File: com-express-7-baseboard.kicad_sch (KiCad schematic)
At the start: 0 parts

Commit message: [#57498] Add KR/SFP+
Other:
- sheet 2xSFP+ ports: added 10GKR_SFP0{10GBaseKR}, 10GKR_SFP1{10GBaseKR}, I2C_{SFP0}{I2C}, I2C_{SFP1}{I2C}, MDIO0{MDIO}, MDIO1{MDIO}, MOD0_ABS, MOD1_ABS, PHY0_{RESET}, PHY1_{RESET}; removed 10GKR_A{10GBaseKR}, 10GKR_B{10GBaseKR}
- sheet Com Express 7 Interfaces ports: added 10G_INT0, 10G_INT1, 10G_PHY_RST01, I2C_{10GLED}{I2C}, I2C_{SFP0}{I2C}, I2C_{SFP1}{I2C}, MDIO0{MDIO}, MDIO1{MDIO}; removed none
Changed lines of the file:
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@@
   (bus_alias "10GBaseKR" (members "TX+" "TX-" "RX+" "RX-"))
   (bus_alias "GbE" (members "MDI3+" "MDI3-" "MDI2+" "MDI2-" "MDI1+" "MDI1-" "MDI0+" "MDI0-" "CTREF"))
+  (bus_alias "MDIO" (members "MDIO" "MDC"))
   (bus_alias "PCIe" (members "TX7+" "TX7-" "TX6+" "TX6-" "TX5+" "TX5-" "TX4+" "TX4-" "TX3+" "TX3-" "TX2+" "TX2-" "TX1+" "TX1-" "TX0+" "TX0-" "RX7+" "RX7-" "RX6+" "RX6-" "RX5+" "RX5-" "RX4+" "RX4-" "RX3+" "RX3-" "RX2+" "RX2-" "RX1+" "RX1-" "RX0+" "RX0-"))
   (bus_alias "USB" (members "D+" "D-"))
@@
   (junction (at 325.12 111.76) (diameter 0) (color 0 0 0 0)
   )
+  (junction (at 121.92 127) (diameter 0) (color 0 0 0 0)
+  )
   (junction (at 327.66 68.58) (diameter 0) (color 0 0 0 0)
   )
   (no_connect (at 251.46 162.56))
-  (no_connect (at 158.75 119.38))
+  (no_connect (at 158.75 97.79))
   (no_connect (at 252.73 175.26))
   (bus (pts (xy 261.62 195.58) (xy 281.94 195.58))
@@
     (stroke (width 0) (type default))
   )
-  (bus (pts (xy 119.38 114.3) (xy 162.56 114.3))
+  (bus (pts (xy 119.38 109.22) (xy 162.56 109.22))
     (stroke (width 0) (type default) (color 255 0 0 1))
   )
@@
     (stroke (width 0) (type default))
   )
+  (bus (pts (xy 119.38 116.84) (xy 162.56 116.84))
+    (stroke (width 0) (type default))
+  )
   (wire (pts (xy 121.92 86.36) (xy 162.56 86.36))
     (stroke (width 0) (type default))
@@
     (stroke (width 0) (type default))
   )
+  (wire (pts (xy 119.38 114.3) (xy 162.56 114.3))
+    (stroke (width 0) (type default))
+  )
   (wire (pts (xy 322.58 68.58) (xy 327.66 68.58))
     (stroke (width 0) (type default))
   )
   (bus (pts (xy 248.92 58.42) (xy 254 58.42))
+    (stroke (width 0) (type default))
+  )
+  (wire (pts (xy 119.38 111.76) (xy 162.56 111.76))
     (stroke (width 0) (type default))
   )
@@
     (stroke (width 0) (type default))
   )
-  (bus (pts (xy 158.75 119.38) (xy 162.56 119.38))
+  (bus (pts (xy 158.75 97.79) (xy 162.56 97.79))
     (stroke (width 0) (type default) (color 255 0 0 1))
   )
@@
     (stroke (width 0) (type default))
   )
+  (bus (pts (xy 119.38 119.38) (xy 162.56 119.38))
+    (stroke (width 0) (type default))
+  )
   (bus (pts (xy 119.38 215.9) (xy 121.92 215.9))
     (stroke (width 0) (type default))
@@
   )
   (bus (pts (xy 67.31 152.4) (xy 67.31 208.28))
+    (stroke (width 0) (type default))
+  )
+  (wire (pts (xy 119.38 127) (xy 121.92 127))
+    (stroke (width 0) (type default))
+  )
+  (wire (pts (xy 121.92 129.54) (xy 121.92 127))
     (stroke (width 0) (type default))
   )
@@
     (stroke (width 0) (type default) (color 194 0 194 1))
   )
+  (wire (pts (xy 119.38 129.54) (xy 121.92 129.54))
+    (stroke (width 0) (type default))
+  )
   (bus (pts (xy 340.36 22.86) (xy 340.36 198.12))
     (stroke (width 0) (type default))
@@
     (stroke (width 0) (type default))
   )
+  (bus (pts (xy 119.38 124.46) (xy 162.56 124.46))
+    (stroke (width 0) (type default))
+  )
   (bus (pts (xy 67.31 208.28) (xy 121.92 208.28))
+    (stroke (width 0) (type default))
+  )
+  (wire (pts (xy 121.92 127) (xy 162.56 127))
     (stroke (width 0) (type default))
   )
@@
     (stroke (width 0) (type default))
   )
+  (bus (pts (xy 119.38 121.92) (xy 162.56 121.92))
+    (stroke (width 0) (type default))
+  )
   (wire (pts (xy 327.66 33.02) (xy 327.66 45.72))
     (stroke (width 0) (type default))
@@
     (stroke (width 0) (type default))
   )
-  (bus (pts (xy 119.38 109.22) (xy 162.56 109.22))
+  (bus (pts (xy 119.38 106.68) (xy 162.56 106.68))
     (stroke (width 0) (type default) (color 255 0 0 1))
   )
@@
       (effects (font (size 1.27 1.27)) (justify left top))
     )
-    (pin "10GKR_A{10GBaseKR}" input (at 119.38 109.22 0)
-      (effects (font (size 1.27 1.27)) (justify right))
-    )
-    (pin "10GKR_B{10GBaseKR}" input (at 119.38 114.3 0)
+    (pin "I2C_{SFP0}{I2C}" input (at 119.38 116.84 0)
+      (effects (font (size 1.27 1.27)) (justify right))
+    )
+    (pin "10GKR_SFP0{10GBaseKR}" input (at 119.38 106.68 0)
+      (effects (font (size 1.27 1.27)) (justify right))
+    )
+    (pin "MOD0_ABS" output (at 119.38 111.76 0)
+      (effects (font (size 1.27 1.27)) (justify right))
+    )
+    (pin "MDIO0{MDIO}" input (at 119.38 121.92 0)
+      (effects (font (size 1.27 1.27)) (justify right))
+    )
+    (pin "PHY0_{RESET}" input (at 119.38 127 0)
+      (effects (font (size 1.27 1.27)) (justify right))
+    )
+    (pin "I2C_{SFP1}{I2C}" input (at 119.38 119.38 0)
+      (effects (font (size 1.27 1.27)) (justify right))
+    )
+    (pin "10GKR_SFP1{10GBaseKR}" input (at 119.38 109.22 0)
+      (effects (font (size 1.27 1.27)) (justify right))
+    )
+    (pin "MOD1_ABS" output (at 119.38 114.3 0)
+      (effects (font (size 1.27 1.27)) (justify right))
+    )
+    (pin "PHY1_{RESET}" input (at 119.38 129.54 0)
+      (effects (font (size 1.27 1.27)) (justify right))
+    )
+    (pin "MDIO1{MDIO}" input (at 119.38 124.46 0)
       (effects (font (size 1.27 1.27)) (justify right))
     )
@@
       (effects (font (size 1.27 1.27)) (justify right))
     )
-    (pin "KR0{10GBaseKR}" output (at 162.56 109.22 180)
-      (effects (font (size 1.27 1.27)) (justify left))
-    )
-    (pin "KR1{10GBaseKR}" output (at 162.56 114.3 180)
+    (pin "KR0{10GBaseKR}" output (at 162.56 106.68 180)
+      (effects (font (size 1.27 1.27)) (justify left))
+    )
+    (pin "KR1{10GBaseKR}" output (at 162.56 109.22 180)
       (effects (font (size 1.27 1.27)) (justify left))
     )
@@
       (effects (font (size 1.27 1.27)) (justify right))
     )
-    (pin "KR2{10GBaseKR}" output (at 162.56 119.38 180)
+    (pin "KR2{10GBaseKR}" output (at 162.56 97.79 180)
       (effects (font (size 1.27 1.27)) (justify left))
     )
@@
       (effects (font (size 1.27 1.27)) (justify left))
     )
+    (pin "10G_INT0" input (at 162.56 111.76 180)
+      (effects (font (size 1.27 1.27)) (justify left))
+    )
+    (pin "10G_INT1" input (at 162.56 114.3 180)
+      (effects (font (size 1.27 1.27)) (justify left))
+    )
+    (pin "I2C_{10GLED}{I2C}" input (at 162.56 140.97 180)
+      (effects (font (size 1.27 1.27)) (justify left))
+    )
+    (pin "I2C_{SFP1}{I2C}" output (at 162.56 119.38 180)
+      (effects (font (size 1.27 1.27)) (justify left))
+    )
+    (pin "I2C_{SFP0}{I2C}" output (at 162.56 116.84 180)
+      (effects (font (size 1.27 1.27)) (justify left))
+    )
+    (pin "MDIO1{MDIO}" output (at 162.56 124.46 180)
+      (effects (font (size 1.27 1.27)) (justify left))
+    )
+    (pin "MDIO0{MDIO}" output (at 162.56 121.92 180)
+      (effects (font (size 1.27 1.27)) (justify left))
+    )
+    (pin "10G_PHY_RST01" output (at 162.56 127 180)
+      (effects (font (size 1.27 1.27)) (justify left))
+    )

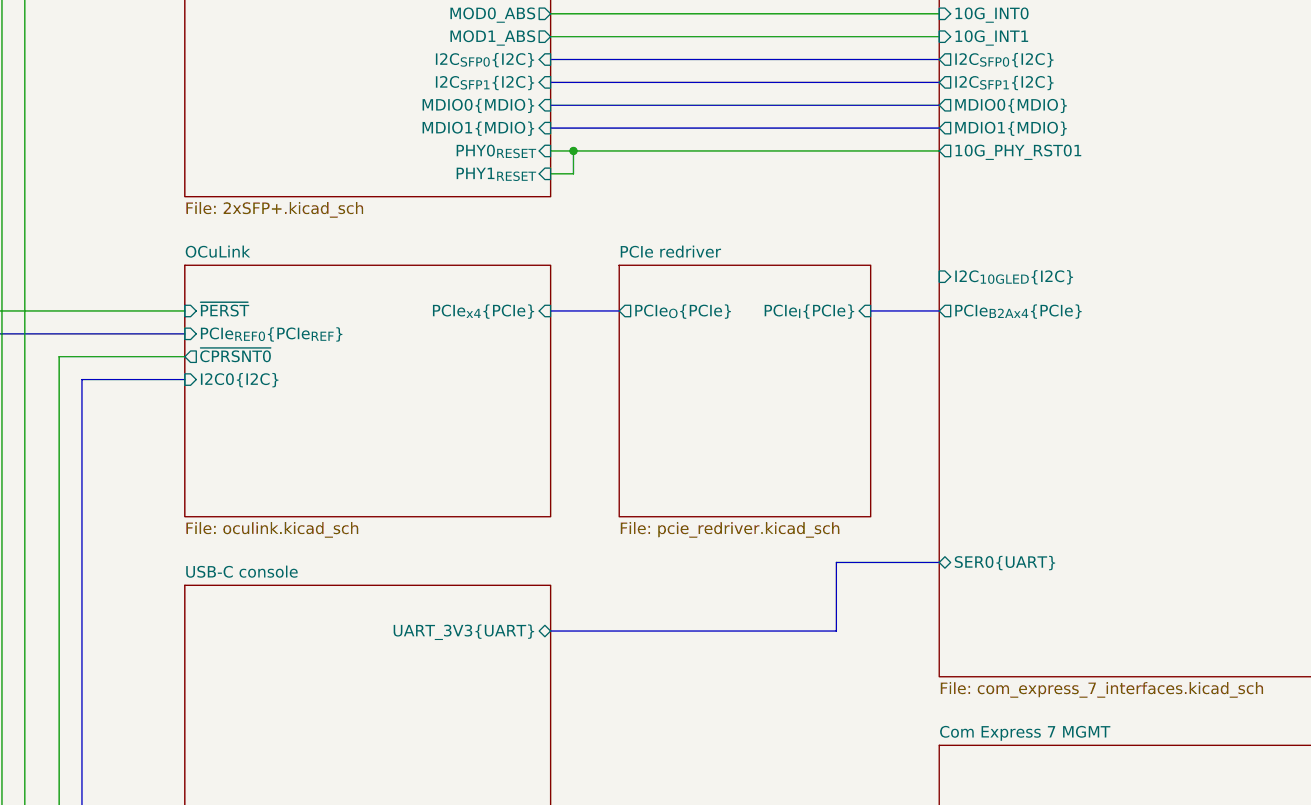
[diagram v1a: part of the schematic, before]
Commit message: [#57498] Add SFP+ indicator LEDs
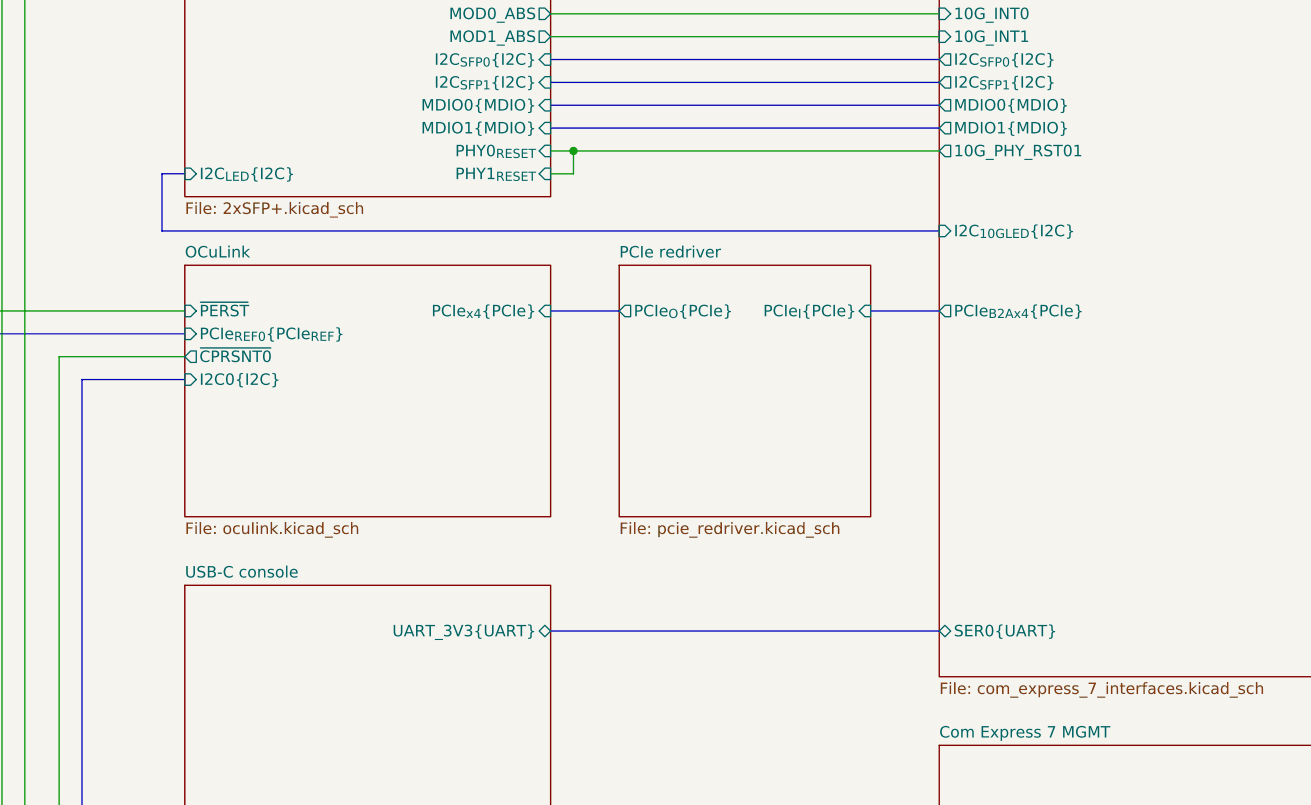
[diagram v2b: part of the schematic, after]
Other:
- sheet 2xSFP+ ports: added I2C_{LED}{I2C}; removed none
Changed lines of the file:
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@@
     (stroke (width 0) (type default))
-  )
-  (bus (pts (xy 162.56 172.72) (xy 151.13 172.72))
-    (stroke (width 0) (type default) (color 255 153 0 1))
   )
   (bus (pts (xy 261.62 177.8) (xy 261.62 195.58))
@@
     (stroke (width 0) (type default) (color 194 0 194 1))
   )
-  (bus (pts (xy 151.13 172.72) (xy 151.13 180.34))
-    (stroke (width 0) (type default) (color 255 153 0 1))
-  )
   (bus (pts (xy 52.07 22.86) (xy 52.07 147.32))
     (stroke (width 0) (type default))
@@
     (stroke (width 0) (type default))
   )
+  (bus (pts (xy 76.2 135.89) (xy 162.56 135.89))
+    (stroke (width 0) (type default))
+  )
+  (bus (pts (xy 76.2 129.54) (xy 76.2 135.89))
+    (stroke (width 0) (type default))
+  )
   (wire (pts (xy 327.66 68.58) (xy 327.66 45.72))
     (stroke (width 0) (type default))
@@
     (stroke (width 0) (type default))
   )
-  (bus (pts (xy 151.13 180.34) (xy 119.38 180.34))
+  (bus (pts (xy 119.38 180.34) (xy 162.56 180.34))
     (stroke (width 0) (type default) (color 255 153 0 1))
   )
@@
     (stroke (width 0) (type default))
   )
+  (bus (pts (xy 78.74 129.54) (xy 76.2 129.54))
+    (stroke (width 0) (type default))
+  )
   (wire (pts (xy 119.38 88.9) (xy 121.92 88.9))
     (stroke (width 0) (type default))
@@
       (effects (font (size 1.27 1.27)) (justify right))
     )
+    (pin "I2C_{LED}{I2C}" input (at 78.74 129.54 180)
+      (effects (font (size 1.27 1.27)) (justify left))
+    )
     (instances
       (project "com-express-7-baseboard"
@@
       (effects (font (size 1.27 1.27)) (justify right))
     )
-    (pin "SER0{UART}" bidirectional (at 162.56 172.72 180)
+    (pin "SER0{UART}" bidirectional (at 162.56 180.34 180)
       (effects (font (size 1.27 1.27)) (justify left))
     )
@@
       (effects (font (size 1.27 1.27)) (justify left))
     )
-    (pin "I2C_{10GLED}{I2C}" input (at 162.56 140.97 180)
-      (effects (font (size 1.27 1.27)) (justify left))
-    )
+    (pin "I2C_{10GLED}{I2C}" input (at 162.56 135.89 180)
+      (effects (font (size 1.27 1.27)) (justify left))
+    )

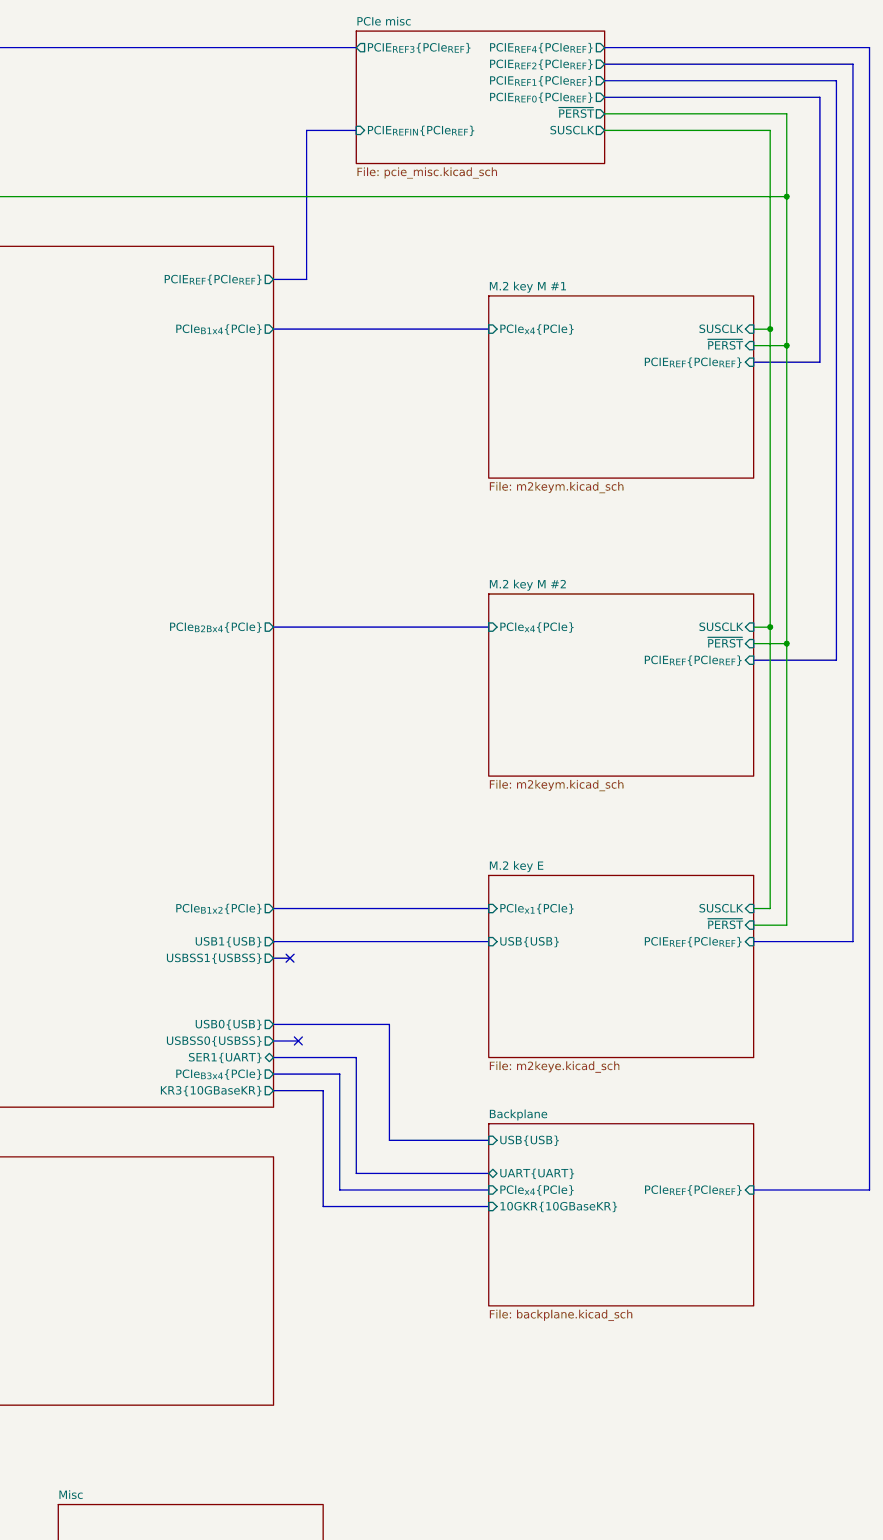
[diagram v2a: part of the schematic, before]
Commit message: [#57498] Add SD card
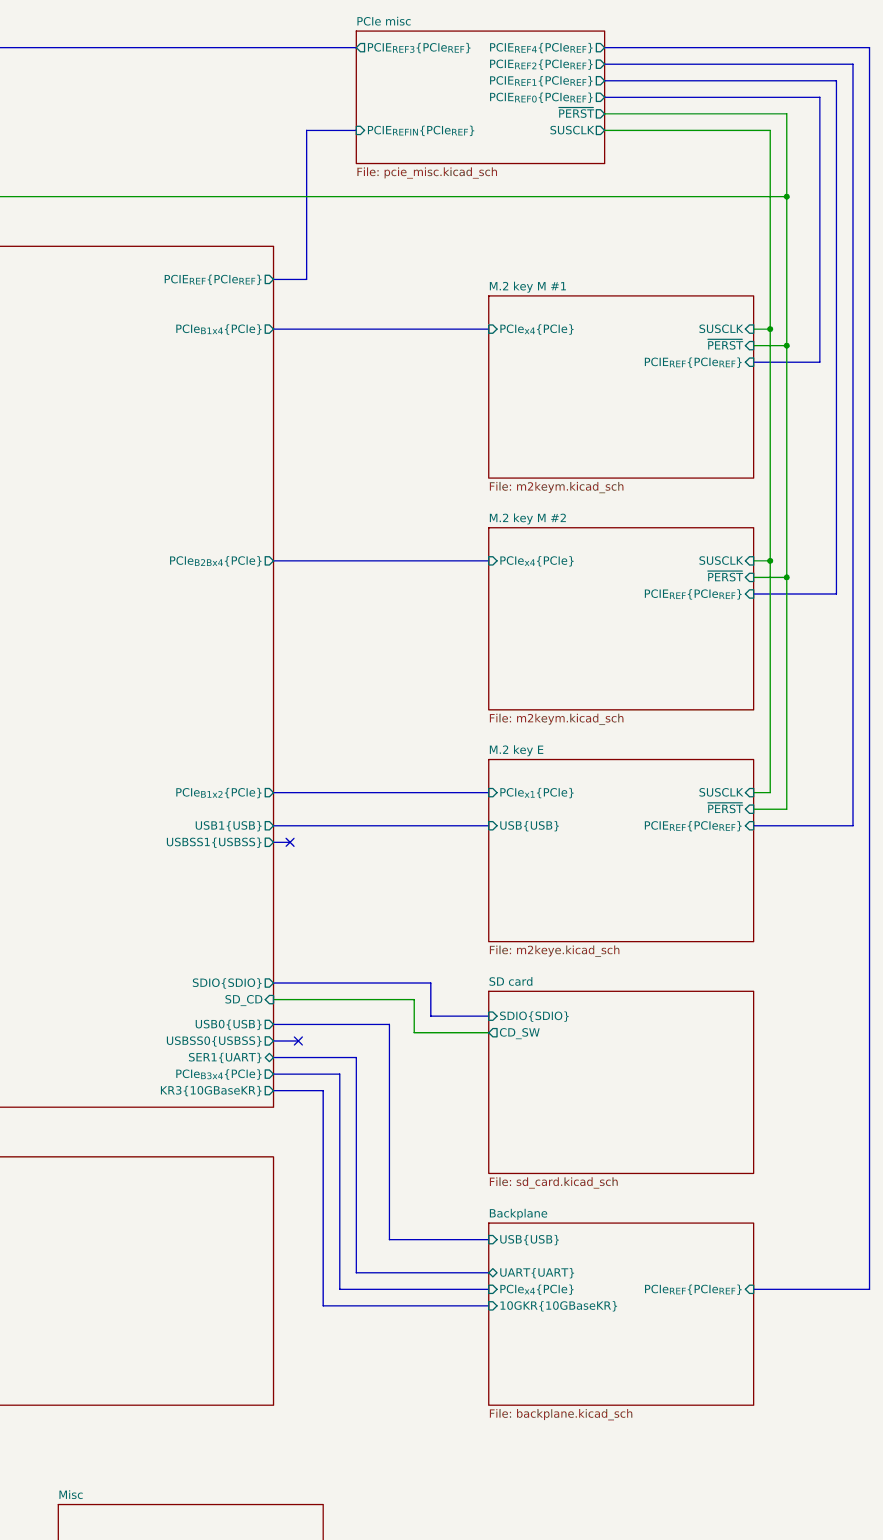
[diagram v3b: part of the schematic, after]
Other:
- added sheet SD card (sd_card.kicad_sch)
- sheet Com Express 7 Interfaces ports: added SDIO{SDIO}, SD_CD; removed none
